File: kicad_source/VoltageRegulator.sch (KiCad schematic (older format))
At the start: 45 parts, among them P2 WR-TBL_691313710002, Q1 IPD90P03P4L- 04, U3 LT1085, U9 IFX91041EJV

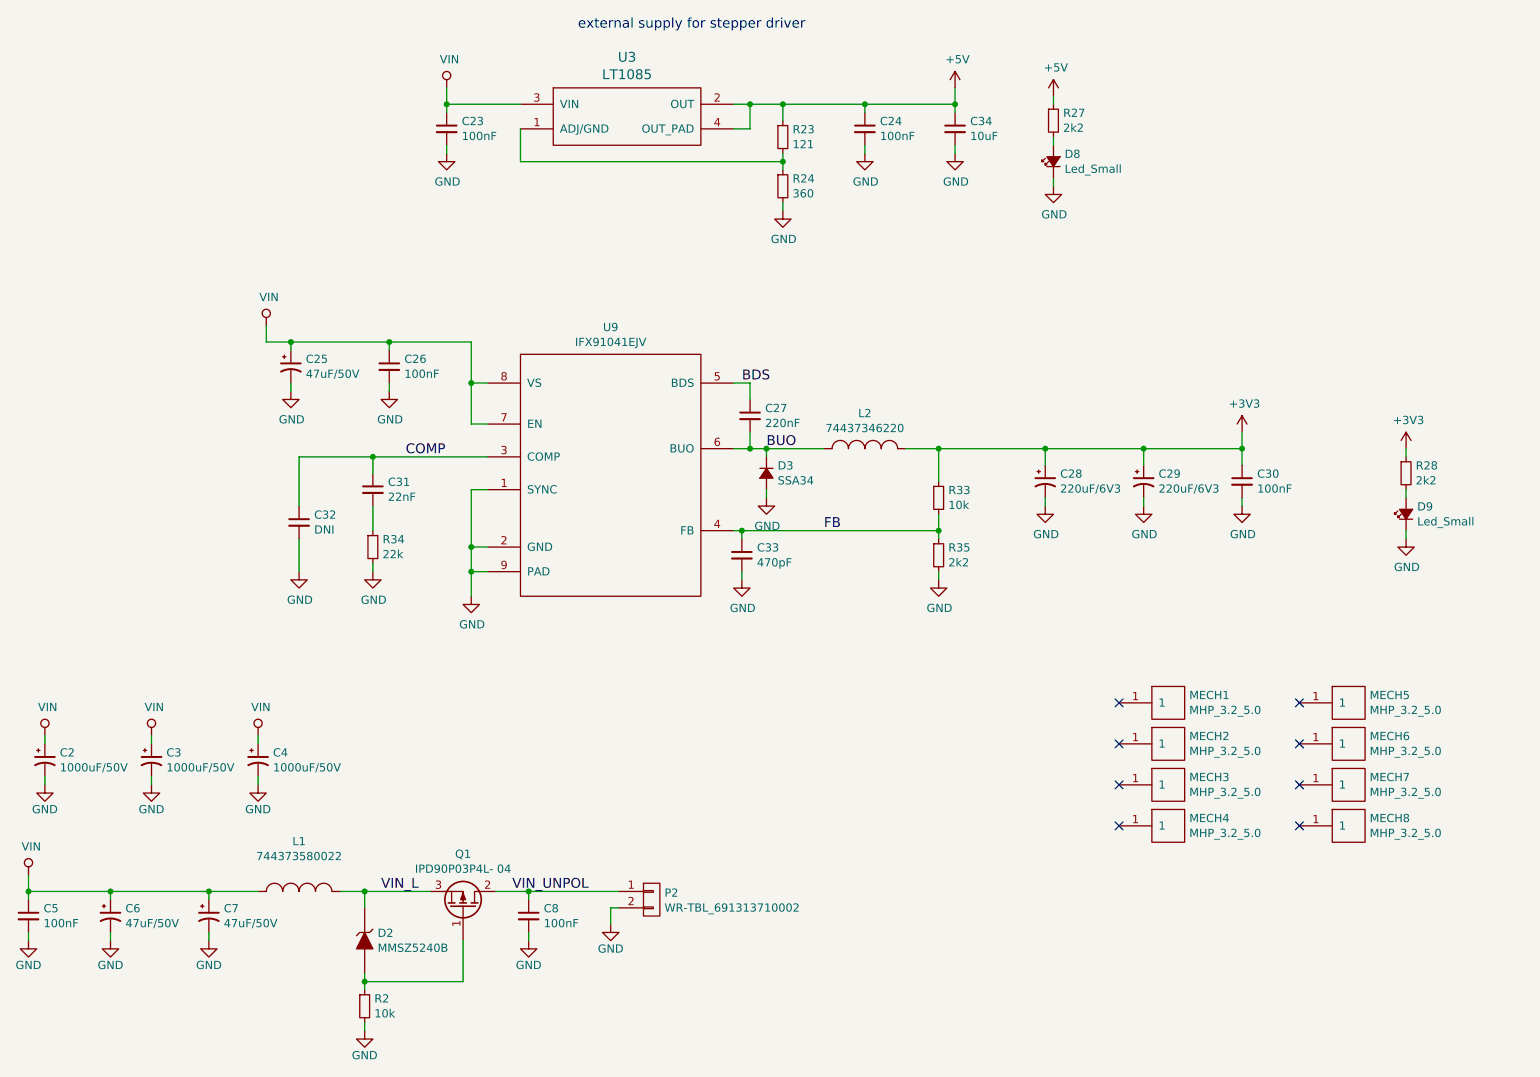
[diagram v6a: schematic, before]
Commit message: updated part numbers
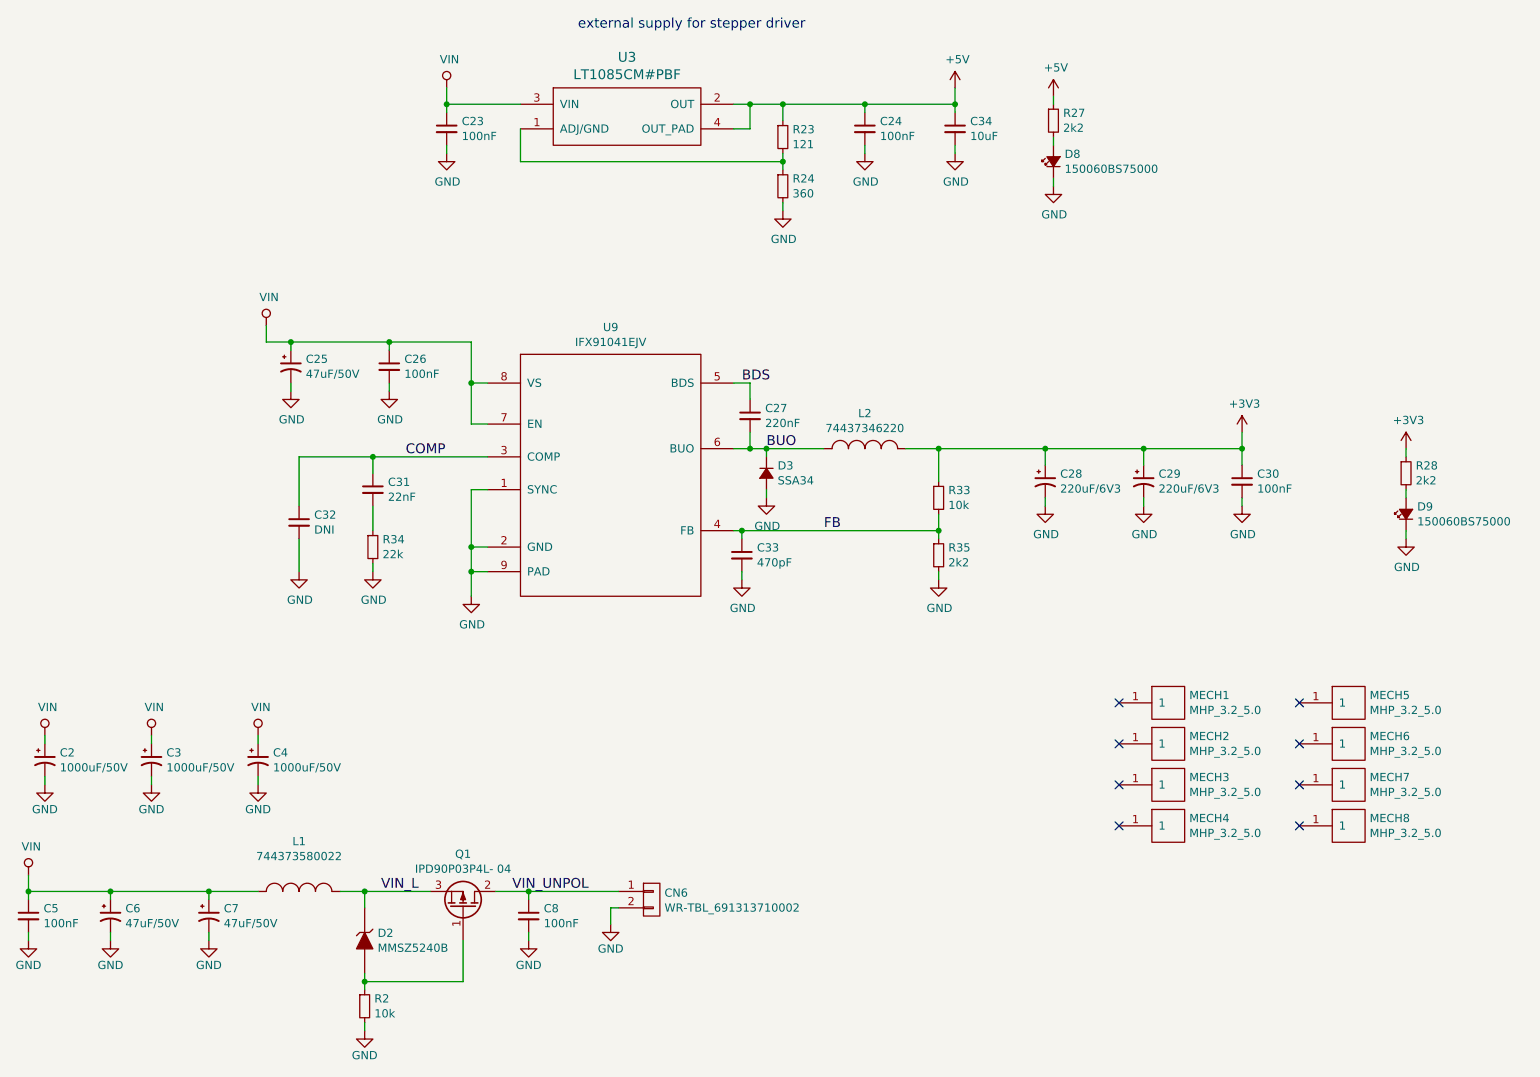
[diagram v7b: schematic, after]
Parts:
- D8, D9: value Led_Small -> 150060BS75000
- U3: value LT1085 -> LT1085CM#PBF
- renumbered P2 to CN6
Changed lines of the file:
@@
 P 5400 6500
 AR Path="/5DE3616E/5DEE0B90" Ref="P?"  Part="1"
-AR Path="/5DE38154/5DEE0B90" Ref="P2"  Part="1"
-F 0 "P2" H 5478 6541 50  0000 L CNN
+AR Path="/5DE38154/5DEE0B90" Ref="CN6"  Part="1"
+F 0 "CN6" H 5478 6541 50  0000 L CNN
 F 1 "WR-TBL_691313710002" H 5478 6450 50  0000 L CNN
 F 2 "CON_wuerth:WR-TBL_691313710002" H 5300 6550 50  0001 C CNN
@@
 P 5250 1750
 F 0 "U3" H 5250 2137 60  0000 C CNN
-F 1 "LT1085" H 5250 2031 60  0000 C CNN
+F 1 "LT1085CM#PBF" H 5250 2031 60  0000 C CNN
 F 2 "SOT_TO:TO-263-3Lead" H 5200 1450 60  0001 C CNN
 F 3 "" H 5250 1750 60  0000 C CNN
@@
 P 10000 4150
 F 0 "D9" V 10046 4082 50  0000 R CNN
-F 1 "Led_Small" V 9955 4082 50  0000 R CNN
+F 1 "150060BS75000" V 9955 4082 50  0000 R CNN
 F 2 "LEDs:LED_0603" V 10000 4150 50  0001 C CNN
 F 3 "" V 10000 4150 50  0000 C CNN
@@
 P 7850 2000
 F 0 "D8" V 7896 1932 50  0000 R CNN
-F 1 "Led_Small" V 7805 1932 50  0000 R CNN
+F 1 "150060BS75000" V 7805 1932 50  0000 R CNN
 F 2 "LEDs:LED_0603" V 7850 2000 50  0001 C CNN
 F 3 "" V 7850 2000 50  0000 C CNN

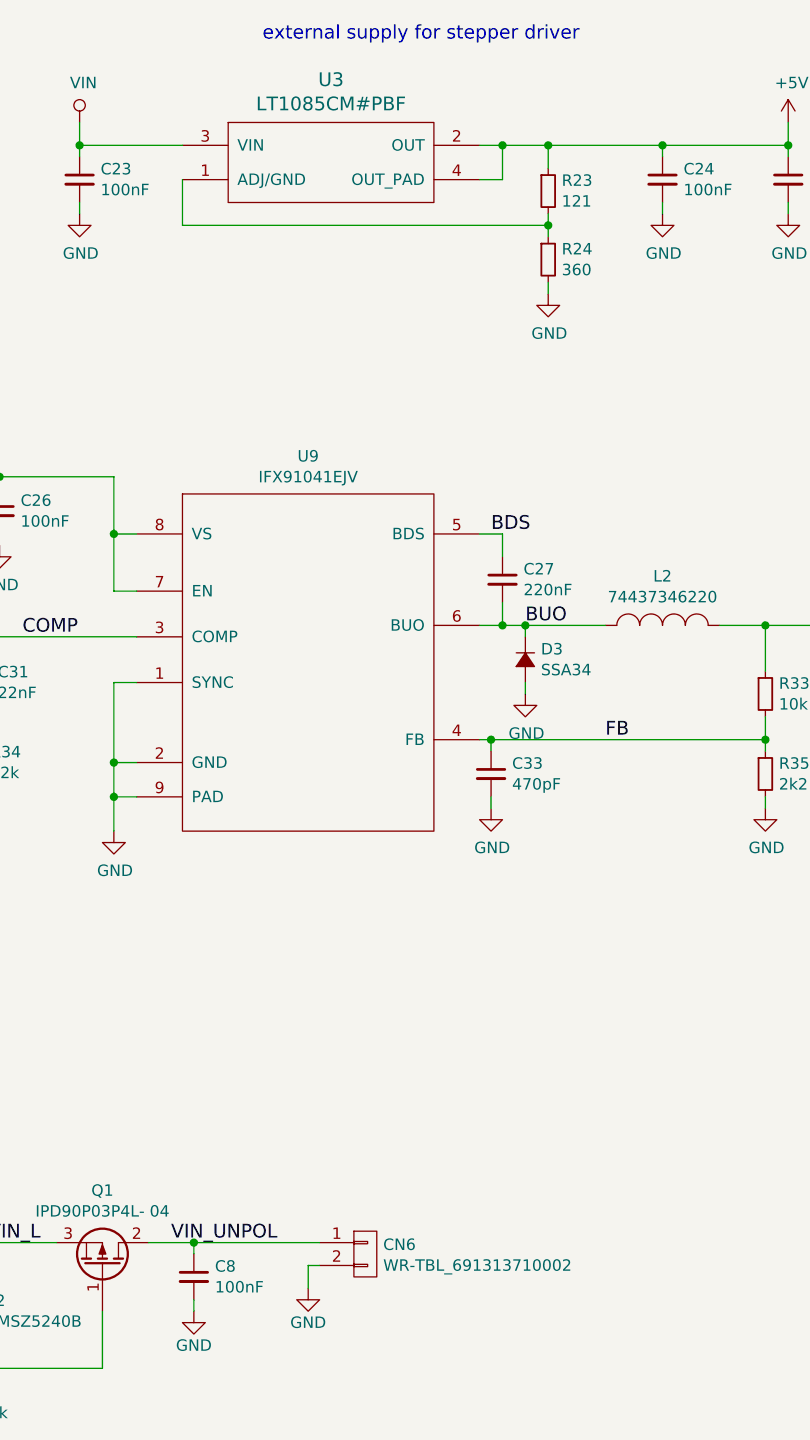
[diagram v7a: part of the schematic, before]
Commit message: updated part numbers
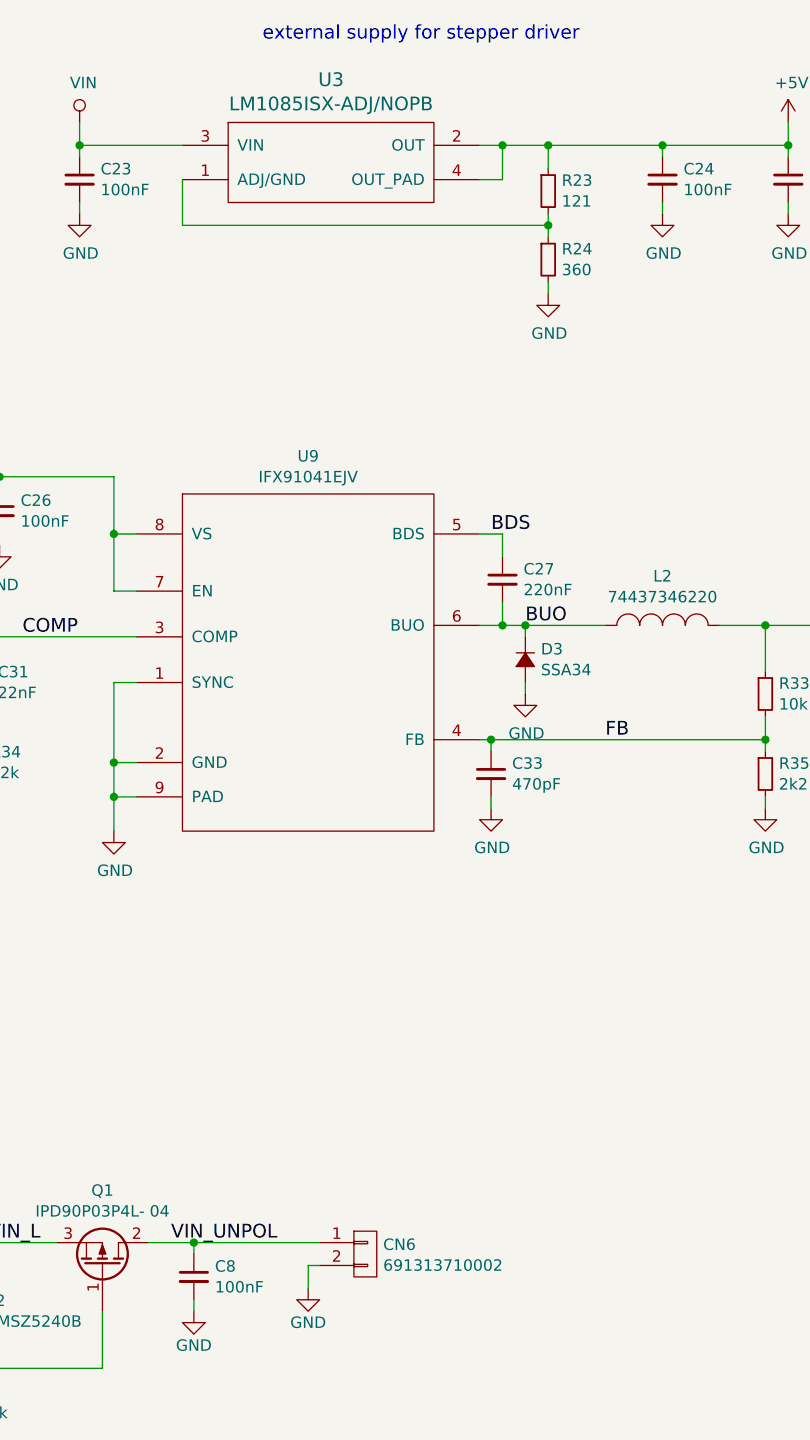
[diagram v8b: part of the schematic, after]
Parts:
- CN6: value WR-TBL_691313710002 -> 691313710002
- U3: value LT1085CM#PBF -> LM1085ISX-ADJ/NOPB
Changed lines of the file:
@@
 AR Path="/5DE38154/5DEE0B90" Ref="CN6"  Part="1"
 F 0 "CN6" H 5478 6541 50  0000 L CNN
-F 1 "WR-TBL_691313710002" H 5478 6450 50  0000 L CNN
+F 1 "691313710002" H 5478 6450 50  0000 L CNN
 F 2 "CON_wuerth:WR-TBL_691313710002" H 5300 6550 50  0001 C CNN
 F 3 "" H 5400 6500 50  0000 C CNN
@@
 P 5250 1750
 F 0 "U3" H 5250 2137 60  0000 C CNN
-F 1 "LT1085CM#PBF" H 5250 2031 60  0000 C CNN
+F 1 "LM1085ISX-ADJ/NOPB" H 5250 2031 60  0000 C CNN
 F 2 "SOT_TO:TO-263-3Lead" H 5200 1450 60  0001 C CNN
 F 3 "" H 5250 1750 60  0000 C CNN
